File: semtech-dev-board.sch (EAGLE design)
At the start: 58 parts, among them Q1 BSS123, U1 SEMTECH_SX1236, U3 MIC5219 3.3V, X1 BU-SMA-G, X2 BU-SMA-G, X3 BU-SMA-G, X4 BU-SMA-G

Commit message: minor edits
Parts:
- Q2: device crystal:CRYSTALSM49 -> low-gain-radio:CRYSTAL2.5X2.0MM
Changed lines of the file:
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@@
 <grid distance="0.1" unitdist="inch" unit="inch" style="lines" multiple="1" display="no" altdistance="0.01" altunitdist="inch" altunit="inch"/>
 <layers>
-<layer number="1" name="Top" color="4" fill="1" visible="no" active="no"/>
-<layer number="2" name="Route2" color="1" fill="3" visible="no" active="no"/>
-<layer number="3" name="Route3" color="4" fill="3" visible="no" active="no"/>
-<layer number="4" name="Route4" color="1" fill="4" visible="no" active="no"/>
-<layer number="5" name="Route5" color="4" fill="4" visible="no" active="no"/>
-<layer number="6" name="Route6" color="1" fill="8" visible="no" active="no"/>
-<layer number="7" name="Route7" color="4" fill="8" visible="no" active="no"/>
-<layer number="8" name="Route8" color="1" fill="2" visible="no" active="no"/>
-<layer number="9" name="Route9" color="4" fill="2" visible="no" active="no"/>
-<layer number="10" name="Route10" color="1" fill="7" visible="no" active="no"/>
-<layer number="11" name="Route11" color="4" fill="7" visible="no" active="no"/>
-<layer number="12" name="Route12" color="1" fill="5" visible="no" active="no"/>
-<layer number="13" name="Route13" color="4" fill="5" visible="no" active="no"/>
-<layer number="14" name="Route14" color="1" fill="6" visible="no" active="no"/>
-<layer number="15" name="Route15" color="4" fill="6" visible="no" active="no"/>
-<layer number="16" name="Bottom" color="1" fill="1" visible="no" active="no"/>
-<layer number="17" name="Pads" color="2" fill="1" visible="no" active="no"/>
-<layer number="18" name="Vias" color="2" fill="1" visible="no" active="no"/>
-<layer number="19" name="Unrouted" color="6" fill="1" visible="no" active="no"/>
-<layer number="20" name="Dimension" color="15" fill="1" visible="no" active="no"/>
-<layer number="21" name="tPlace" color="7" fill="1" visible="no" active="no"/>
-<layer number="22" name="bPlace" color="7" fill="1" visible="no" active="no"/>
-<layer number="23" name="tOrigins" color="15" fill="1" visible="no" active="no"/>
-<layer number="24" name="bOrigins" color="15" fill="1" visible="no" active="no"/>
-<layer number="25" name="tNames" color="7" fill="1" visible="no" active="no"/>
-<layer number="26" name="bNames" color="7" fill="1" visible="no" active="no"/>
-<layer number="27" name="tValues" color="7" fill="1" visible="no" active="no"/>
-<layer number="28" name="bValues" color="7" fill="1" visible="no" active="no"/>
+<layer number="1" name="Top" color="4" fill="1" visible="yes" active="no"/>
+<layer number="2" name="Route2" color="1" fill="3" visible="yes" active="no"/>
+<layer number="3" name="Route3" color="4" fill="3" visible="yes" active="no"/>
+<layer number="4" name="Route4" color="1" fill="4" visible="yes" active="no"/>
+<layer number="5" name="Route5" color="4" fill="4" visible="yes" active="no"/>
+<layer number="6" name="Route6" color="1" fill="8" visible="yes" active="no"/>
+<layer number="7" name="Route7" color="4" fill="8" visible="yes" active="no"/>
+<layer number="8" name="Route8" color="1" fill="2" visible="yes" active="no"/>
+<layer number="9" name="Route9" color="4" fill="2" visible="yes" active="no"/>
+<layer number="10" name="Route10" color="1" fill="7" visible="yes" active="no"/>
+<layer number="11" name="Route11" color="4" fill="7" visible="yes" active="no"/>
+<layer number="12" name="Route12" color="1" fill="5" visible="yes" active="no"/>
+<layer number="13" name="Route13" color="4" fill="5" visible="yes" active="no"/>
+<layer number="14" name="Route14" color="1" fill="6" visible="yes" active="no"/>
+<layer number="15" name="Route15" color="4" fill="6" visible="yes" active="no"/>
+<layer number="16" name="Bottom" color="1" fill="1" visible="yes" active="no"/>
+<layer number="17" name="Pads" color="2" fill="1" visible="yes" active="no"/>
+<layer number="18" name="Vias" color="2" fill="1" visible="yes" active="no"/>
+<layer number="19" name="Unrouted" color="6" fill="1" visible="yes" active="no"/>
+<layer number="20" name="Dimension" color="15" fill="1" visible="yes" active="no"/>
+<layer number="21" name="tPlace" color="7" fill="1" visible="yes" active="no"/>
+<layer number="22" name="bPlace" color="7" fill="1" visible="yes" active="no"/>
+<layer number="23" name="tOrigins" color="15" fill="1" visible="yes" active="no"/>
+<layer number="24" name="bOrigins" color="15" fill="1" visible="yes" active="no"/>
+<layer number="25" name="tNames" color="7" fill="1" visible="yes" active="no"/>
+<layer number="26" name="bNames" color="7" fill="1" visible="yes" active="no"/>
+<layer number="27" name="tValues" color="7" fill="1" visible="yes" active="no"/>
+<layer number="28" name="bValues" color="7" fill="1" visible="yes" active="no"/>
 <layer number="29" name="tStop" color="7" fill="3" visible="no" active="no"/>
 <layer number="30" name="bStop" color="7" fill="6" visible="no" active="no"/>
@@
 <layer number="35" name="tGlue" color="7" fill="4" visible="no" active="no"/>
 <layer number="36" name="bGlue" color="7" fill="5" visible="no" active="no"/>
-<layer number="37" name="tTest" color="7" fill="1" visible="no" active="no"/>
-<layer number="38" name="bTest" color="7" fill="1" visible="no" active="no"/>
+<layer number="37" name="tTest" color="7" fill="1" visible="yes" active="no"/>
+<layer number="38" name="bTest" color="7" fill="1" visible="yes" active="no"/>
 <layer number="39" name="tKeepout" color="4" fill="11" visible="no" active="no"/>
 <layer number="40" name="bKeepout" color="1" fill="11" visible="no" active="no"/>
@@
 <layer number="44" name="Drills" color="7" fill="1" visible="no" active="no"/>
 <layer number="45" name="Holes" color="7" fill="1" visible="no" active="no"/>
-<layer number="46" name="Milling" color="3" fill="1" visible="no" active="no"/>
-<layer number="47" name="Measures" color="7" fill="1" visible="no" active="no"/>
-<layer number="48" name="Document" color="7" fill="1" visible="no" active="no"/>
-<layer number="49" name="Reference" color="7" fill="1" visible="no" active="no"/>
-<layer number="50" name="dxf" color="7" fill="1" visible="no" active="no"/>
-<layer number="51" name="tDocu" color="7" fill="1" visible="no" active="no"/>
-<layer number="52" name="bDocu" color="7" fill="1" visible="no" active="no"/>
-<layer number="53" name="tGND_GNDA" color="7" fill="1" visible="no" active="no"/>
-<layer number="54" name="bGND_GNDA" color="7" fill="1" visible="no" active="no"/>
-<layer number="56" name="wert" color="7" fill="1" visible="no" active="no"/>
-<layer number="57" name="tCAD" color="7" fill="1" visible="no" active="no"/>
-<layer number="58" name="b3D" color="7" fill="1" visible="no" active="no"/>
-<layer number="59" name="Invisible" color="7" fill="1" visible="no" active="no"/>
-<layer number="60" name="bCarbon" color="7" fill="1" visible="no" active="no"/>
-<layer number="61" name="stand" color="7" fill="1" visible="no" active="no"/>
+<layer number="46" name="Milling" color="3" fill="1" visible="yes" active="no"/>
+<layer number="47" name="Measures" color="7" fill="1" visible="yes" active="no"/>
+<layer number="48" name="Document" color="7" fill="1" visible="yes" active="no"/>
+<layer number="49" name="Reference" color="7" fill="1" visible="yes" active="no"/>
+<layer number="50" name="dxf" color="7" fill="1" visible="yes" active="no"/>
+<layer number="51" name="tDocu" color="7" fill="1" visible="yes" active="no"/>
+<layer number="52" name="bDocu" color="7" fill="1" visible="yes" active="no"/>
+<layer number="53" name="tGND_GNDA" color="7" fill="1" visible="yes" active="no"/>
+<layer number="54" name="bGND_GNDA" color="7" fill="1" visible="yes" active="no"/>
+<layer number="56" name="wert" color="7" fill="1" visible="yes" active="no"/>
+<layer number="57" name="tCAD" color="7" fill="1" visible="yes" active="no"/>
+<layer number="58" name="b3D" color="7" fill="1" visible="yes" active="no"/>
+<layer number="59" name="Invisible" color="7" fill="1" visible="yes" active="no"/>
+<layer number="60" name="bCarbon" color="7" fill="1" visible="yes" active="no"/>
+<layer number="61" name="stand" color="7" fill="1" visible="yes" active="no"/>
 <layer number="90" name="Modules" color="5" fill="1" visible="yes" active="yes"/>
 <layer number="91" name="Nets" color="2" fill="1" visible="yes" active="yes"/>
@@
 <part name="X2" library="con-coax" deviceset="BU-SMA-G" device=""/>
 <part name="X3" library="con-coax" deviceset="BU-SMA-G" device=""/>
-<part name="Q2" library="crystal" deviceset="CRYSTAL" device="SM49"/>
+<part name="Q2" library="low-gain-radio" deviceset="CRYSTAL" device="2.5X2.0MM"/>
 <part name="S1" library="switch" deviceset="RDT1034" device=""/>
 <part name="GND2" library="supply1" deviceset="GND" device=""/>

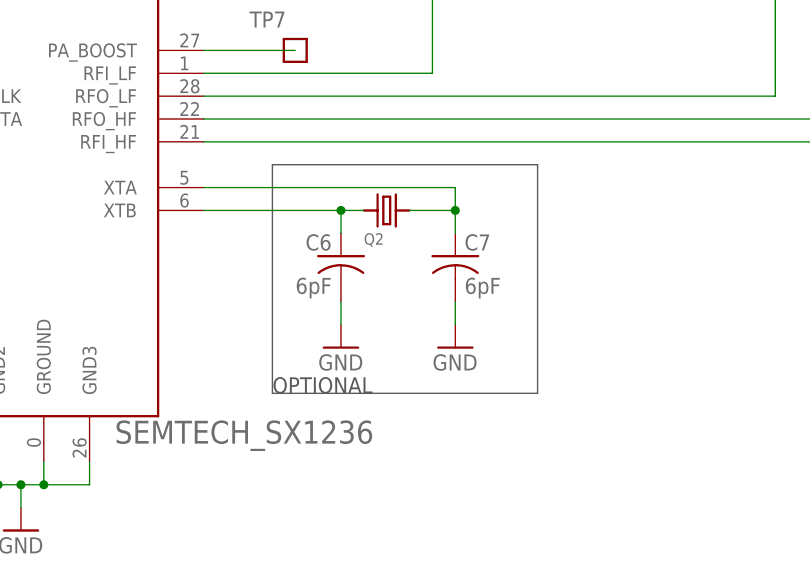
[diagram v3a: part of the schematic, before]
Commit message: started routing, adjusted placement, named nets
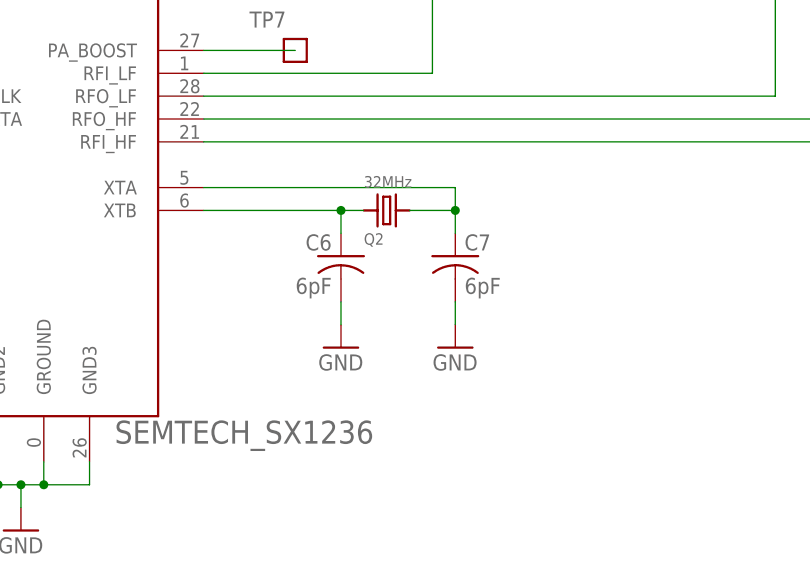
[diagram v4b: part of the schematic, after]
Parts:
- Q2: value (none) -> 32MHz
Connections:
- net N$1 renamed LED-
- net N$15 renamed HFO_PA_HEAD
- net N$2 renamed XTALA
- net N$24 renamed LFO_PA_HEAD
- net N$6 renamed LED+
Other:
- note removed: "OPTIONAL"
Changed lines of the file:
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@@
 <grid distance="0.1" unitdist="inch" unit="inch" style="lines" multiple="1" display="no" altdistance="0.01" altunitdist="inch" altunit="inch"/>
 <layers>
-<layer number="1" name="Top" color="4" fill="1" visible="yes" active="no"/>
-<layer number="2" name="Route2" color="1" fill="3" visible="yes" active="no"/>
-<layer number="3" name="Route3" color="4" fill="3" visible="yes" active="no"/>
-<layer number="4" name="Route4" color="1" fill="4" visible="yes" active="no"/>
-<layer number="5" name="Route5" color="4" fill="4" visible="yes" active="no"/>
-<layer number="6" name="Route6" color="1" fill="8" visible="yes" active="no"/>
-<layer number="7" name="Route7" color="4" fill="8" visible="yes" active="no"/>
-<layer number="8" name="Route8" color="1" fill="2" visible="yes" active="no"/>
-<layer number="9" name="Route9" color="4" fill="2" visible="yes" active="no"/>
-<layer number="10" name="Route10" color="1" fill="7" visible="yes" active="no"/>
-<layer number="11" name="Route11" color="4" fill="7" visible="yes" active="no"/>
-<layer number="12" name="Route12" color="1" fill="5" visible="yes" active="no"/>
-<layer number="13" name="Route13" color="4" fill="5" visible="yes" active="no"/>
-<layer number="14" name="Route14" color="1" fill="6" visible="yes" active="no"/>
-<layer number="15" name="Route15" color="4" fill="6" visible="yes" active="no"/>
-<layer number="16" name="Bottom" color="1" fill="1" visible="yes" active="no"/>
-<layer number="17" name="Pads" color="2" fill="1" visible="yes" active="no"/>
-<layer number="18" name="Vias" color="2" fill="1" visible="yes" active="no"/>
-<layer number="19" name="Unrouted" color="6" fill="1" visible="yes" active="no"/>
-<layer number="20" name="Dimension" color="15" fill="1" visible="yes" active="no"/>
-<layer number="21" name="tPlace" color="7" fill="1" visible="yes" active="no"/>
-<layer number="22" name="bPlace" color="7" fill="1" visible="yes" active="no"/>
-<layer number="23" name="tOrigins" color="15" fill="1" visible="yes" active="no"/>
-<layer number="24" name="bOrigins" color="15" fill="1" visible="yes" active="no"/>
-<layer number="25" name="tNames" color="7" fill="1" visible="yes" active="no"/>
-<layer number="26" name="bNames" color="7" fill="1" visible="yes" active="no"/>
-<layer number="27" name="tValues" color="7" fill="1" visible="yes" active="no"/>
-<layer number="28" name="bValues" color="7" fill="1" visible="yes" active="no"/>
+<layer number="1" name="Top" color="4" fill="1" visible="no" active="no"/>
+<layer number="2" name="Route2" color="1" fill="3" visible="no" active="no"/>
+<layer number="3" name="Route3" color="4" fill="3" visible="no" active="no"/>
+<layer number="4" name="Route4" color="1" fill="4" visible="no" active="no"/>
+<layer number="5" name="Route5" color="4" fill="4" visible="no" active="no"/>
+<layer number="6" name="Route6" color="1" fill="8" visible="no" active="no"/>
+<layer number="7" name="Route7" color="4" fill="8" visible="no" active="no"/>
+<layer number="8" name="Route8" color="1" fill="2" visible="no" active="no"/>
+<layer number="9" name="Route9" color="4" fill="2" visible="no" active="no"/>
+<layer number="10" name="Route10" color="1" fill="7" visible="no" active="no"/>
+<layer number="11" name="Route11" color="4" fill="7" visible="no" active="no"/>
+<layer number="12" name="Route12" color="1" fill="5" visible="no" active="no"/>
+<layer number="13" name="Route13" color="4" fill="5" visible="no" active="no"/>
+<layer number="14" name="Route14" color="1" fill="6" visible="no" active="no"/>
+<layer number="15" name="Route15" color="4" fill="6" visible="no" active="no"/>
+<layer number="16" name="Bottom" color="1" fill="1" visible="no" active="no"/>
+<layer number="17" name="Pads" color="2" fill="1" visible="no" active="no"/>
+<layer number="18" name="Vias" color="2" fill="1" visible="no" active="no"/>
+<layer number="19" name="Unrouted" color="6" fill="1" visible="no" active="no"/>
+<layer number="20" name="Dimension" color="15" fill="1" visible="no" active="no"/>
+<layer number="21" name="tPlace" color="7" fill="1" visible="no" active="no"/>
+<layer number="22" name="bPlace" color="7" fill="1" visible="no" active="no"/>
+<layer number="23" name="tOrigins" color="15" fill="1" visible="no" active="no"/>
+<layer number="24" name="bOrigins" color="15" fill="1" visible="no" active="no"/>
+<layer number="25" name="tNames" color="7" fill="1" visible="no" active="no"/>
+<layer number="26" name="bNames" color="7" fill="1" visible="no" active="no"/>
+<layer number="27" name="tValues" color="7" fill="1" visible="no" active="no"/>
+<layer number="28" name="bValues" color="7" fill="1" visible="no" active="no"/>
 <layer number="29" name="tStop" color="7" fill="3" visible="no" active="no"/>
 <layer number="30" name="bStop" color="7" fill="6" visible="no" active="no"/>
@@
 <layer number="35" name="tGlue" color="7" fill="4" visible="no" active="no"/>
 <layer number="36" name="bGlue" color="7" fill="5" visible="no" active="no"/>
-<layer number="37" name="tTest" color="7" fill="1" visible="yes" active="no"/>
-<layer number="38" name="bTest" color="7" fill="1" visible="yes" active="no"/>
+<layer number="37" name="tTest" color="7" fill="1" visible="no" active="no"/>
+<layer number="38" name="bTest" color="7" fill="1" visible="no" active="no"/>
 <layer number="39" name="tKeepout" color="4" fill="11" visible="no" active="no"/>
 <layer number="40" name="bKeepout" color="1" fill="11" visible="no" active="no"/>
@@
 <layer number="44" name="Drills" color="7" fill="1" visible="no" active="no"/>
 <layer number="45" name="Holes" color="7" fill="1" visible="no" active="no"/>
-<layer number="46" name="Milling" color="3" fill="1" visible="yes" active="no"/>
-<layer number="47" name="Measures" color="7" fill="1" visible="yes" active="no"/>
-<layer number="48" name="Document" color="7" fill="1" visible="yes" active="no"/>
-<layer number="49" name="Reference" color="7" fill="1" visible="yes" active="no"/>
-<layer number="50" name="dxf" color="7" fill="1" visible="yes" active="no"/>
-<layer number="51" name="tDocu" color="7" fill="1" visible="yes" active="no"/>
-<layer number="52" name="bDocu" color="7" fill="1" visible="yes" active="no"/>
-<layer number="53" name="tGND_GNDA" color="7" fill="1" visible="yes" active="no"/>
-<layer number="54" name="bGND_GNDA" color="7" fill="1" visible="yes" active="no"/>
-<layer number="56" name="wert" color="7" fill="1" visible="yes" active="no"/>
-<layer number="57" name="tCAD" color="7" fill="1" visible="yes" active="no"/>
-<layer number="58" name="b3D" color="7" fill="1" visible="yes" active="no"/>
-<layer number="59" name="Invisible" color="7" fill="1" visible="yes" active="no"/>
-<layer number="60" name="bCarbon" color="7" fill="1" visible="yes" active="no"/>
-<layer number="61" name="stand" color="7" fill="1" visible="yes" active="no"/>
+<layer number="46" name="Milling" color="3" fill="1" visible="no" active="no"/>
+<layer number="47" name="Measures" color="7" fill="1" visible="no" active="no"/>
+<layer number="48" name="Document" color="7" fill="1" visible="no" active="no"/>
+<layer number="49" name="Reference" color="7" fill="1" visible="no" active="no"/>
+<layer number="50" name="dxf" color="7" fill="1" visible="no" active="no"/>
+<layer number="51" name="tDocu" color="7" fill="1" visible="no" active="no"/>
+<layer number="52" name="bDocu" color="7" fill="1" visible="no" active="no"/>
+<layer number="53" name="tGND_GNDA" color="7" fill="1" visible="no" active="no"/>
+<layer number="54" name="bGND_GNDA" color="7" fill="1" visible="no" active="no"/>
+<layer number="56" name="wert" color="7" fill="1" visible="no" active="no"/>
+<layer number="57" name="tCAD" color="7" fill="1" visible="no" active="no"/>
+<layer number="58" name="b3D" color="7" fill="1" visible="no" active="no"/>
+<layer number="59" name="Invisible" color="7" fill="1" visible="no" active="no"/>
+<layer number="60" name="bCarbon" color="7" fill="1" visible="no" active="no"/>
+<layer number="61" name="stand" color="7" fill="1" visible="no" active="no"/>
 <layer number="90" name="Modules" color="5" fill="1" visible="yes" active="yes"/>
 <layer number="91" name="Nets" color="2" fill="1" visible="yes" active="yes"/>
@@
 <part name="X2" library="con-coax" deviceset="BU-SMA-G" device=""/>
 <part name="X3" library="con-coax" deviceset="BU-SMA-G" device=""/>
-<part name="Q2" library="low-gain-radio" deviceset="CRYSTAL" device="2.5X2.0MM"/>
+<part name="Q2" library="low-gain-radio" deviceset="CRYSTAL" device="2.5X2.0MM" value="32MHz"/>
 <part name="S1" library="switch" deviceset="RDT1034" device=""/>
 <part name="GND2" library="supply1" deviceset="GND" device=""/>
@@
 <sheet>
 <plain>
-<wire x1="93.98" y1="22.86" x2="93.98" y2="48.26" width="0.1524" layer="97"/>
-<wire x1="93.98" y1="48.26" x2="123.444" y2="48.26" width="0.1524" layer="97"/>
-<wire x1="123.444" y1="48.26" x2="123.444" y2="22.86" width="0.1524" layer="97"/>
-<wire x1="123.444" y1="22.86" x2="93.98" y2="22.86" width="0.1524" layer="97"/>
-<text x="93.98" y="22.86" size="1.778" layer="97">OPTIONAL</text>
 <wire x1="137.16" y1="172.72" x2="254" y2="172.72" width="0.1524" layer="97"/>
 <wire x1="254" y1="172.72" x2="254" y2="220.98" width="0.1524" layer="97"/>
@@
 </segment>
 </net>
-<net name="N$1" class="0">
+<net name="LED-" class="0">
 <segment>
 <pinref part="Q1" gate="G$1" pin="D"/>
@@
 </segment>
 </net>
-<net name="N$6" class="0">
+<net name="LED+" class="0">
 <segment>
 <pinref part="LED1" gate="G$1" pin="A"/>
@@
 </segment>
 </net>
-<net name="N$2" class="0">
+<net name="XTALA" class="0">
 <segment>
 <pinref part="U1" gate="G$1" pin="XTA"/>
@@
 </segment>
 </net>
-<net name="N$15" class="0">
+<net name="HFO_PA_HEAD" class="0">
 <segment>
 <pinref part="C9" gate="G$1" pin="1"/>
@@
 </segment>
 </net>
-<net name="N$24" class="0">
+<net name="LFO_PA_HEAD" class="0">
 <segment>
 <pinref part="C8" gate="G$1" pin="1"/>
